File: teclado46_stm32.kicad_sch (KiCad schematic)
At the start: 12 parts, among them J2 78171-0004, U1 XC6206PxxxMR, U2 STM32G474CETx, U4 W25Q128JVS

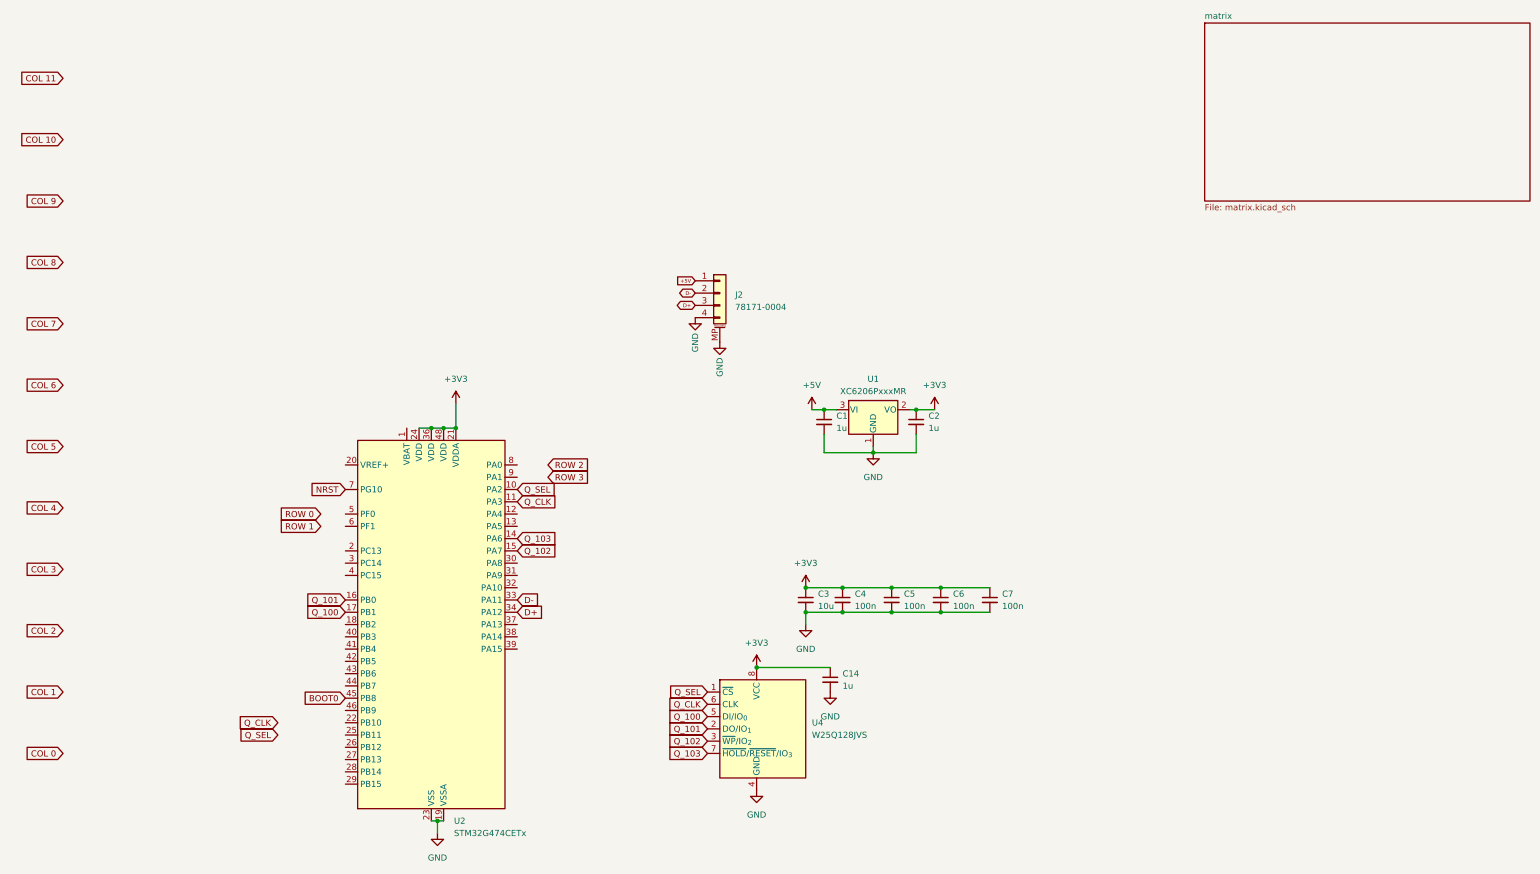
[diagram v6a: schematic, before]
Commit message: chore: routed columns
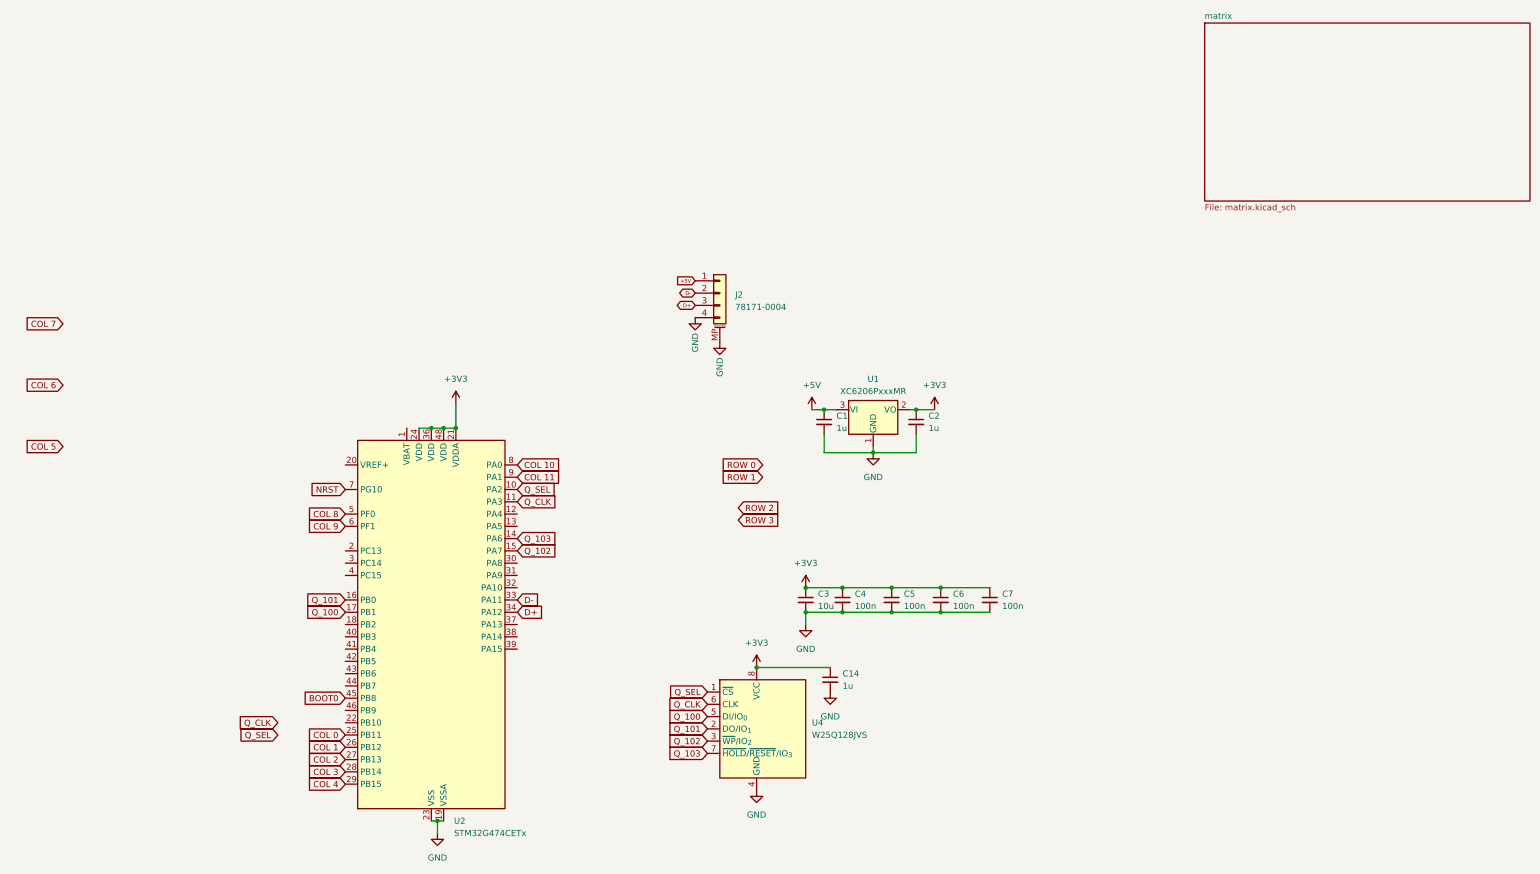
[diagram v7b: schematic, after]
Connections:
- net COL 0: now also U2.25 (PB11)
- net COL 1: now also U2.26 (PB12)
- net COL 10: now also U2.8 (PA0)
- net COL 11: now also U2.9 (PA1)
- net COL 2: now also U2.27 (PB13)
- net COL 3: now also U2.28 (PB14)
- net COL 4: now also U2.29 (PB15)
- net COL 8: now also U2.5 (PF0)
- net COL 9: now also U2.6 (PF1)
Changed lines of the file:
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@@
 	(global_label "COL 2"
 		(shape input)
-		(at -25.4 144.78 180)
-		(fields_autoplaced yes)
-		(effects
-			(font
-				(size 1.27 1.27)
-			)
-			(justify right)
-		)
-		(property "Intersheetrefs" "${INTERSHEET_REFS}"
-			(at -34.1909 144.78 0)
+		(at 33.02 171.45 180)
+		(fields_autoplaced yes)
+		(effects
+			(font
+				(size 1.27 1.27)
+			)
+			(justify right)
+		)
+		(property "Intersheetrefs" "${INTERSHEET_REFS}"
+			(at 24.2291 171.45 0)
 			(effects
 				(font
@@
 	(global_label "ROW 1"
 		(shape input)
-		(at 27.94 123.19 180)
-		(fields_autoplaced yes)
-		(effects
-			(font
-				(size 1.27 1.27)
-			)
-			(justify right)
-		)
-		(property "Intersheetrefs" "${INTERSHEET_REFS}"
-			(at 18.7258 123.19 0)
+		(at 119.38 113.03 180)
+		(fields_autoplaced yes)
+		(effects
+			(font
+				(size 1.27 1.27)
+			)
+			(justify right)
+		)
+		(property "Intersheetrefs" "${INTERSHEET_REFS}"
+			(at 110.1658 113.03 0)
 			(effects
 				(font
@@
 	(global_label "COL 3"
 		(shape input)
-		(at -25.4 132.08 180)
-		(fields_autoplaced yes)
-		(effects
-			(font
-				(size 1.27 1.27)
-			)
-			(justify right)
-		)
-		(property "Intersheetrefs" "${INTERSHEET_REFS}"
-			(at -34.1909 132.08 0)
+		(at 33.02 173.99 180)
+		(fields_autoplaced yes)
+		(effects
+			(font
+				(size 1.27 1.27)
+			)
+			(justify right)
+		)
+		(property "Intersheetrefs" "${INTERSHEET_REFS}"
+			(at 24.2291 173.99 0)
 			(effects
 				(font
@@
 	(global_label "COL 10"
 		(shape input)
-		(at -25.4 43.18 180)
-		(fields_autoplaced yes)
-		(effects
-			(font
-				(size 1.27 1.27)
-			)
-			(justify right)
-		)
-		(property "Intersheetrefs" "${INTERSHEET_REFS}"
-			(at -35.4004 43.18 0)
-			(effects
-				(font
-					(size 1.27 1.27)
-				)
-				(justify right)
+		(at 68.58 110.49 0)
+		(fields_autoplaced yes)
+		(effects
+			(font
+				(size 1.27 1.27)
+			)
+			(justify left)
+		)
+		(property "Intersheetrefs" "${INTERSHEET_REFS}"
+			(at 78.5804 110.49 0)
+			(effects
+				(font
+					(size 1.27 1.27)
+				)
+				(justify left)
 				(hide yes)
 			)
@@
 	(global_label "COL 1"
 		(shape input)
-		(at -25.4 157.48 180)
-		(fields_autoplaced yes)
-		(effects
-			(font
-				(size 1.27 1.27)
-			)
-			(justify right)
-		)
-		(property "Intersheetrefs" "${INTERSHEET_REFS}"
-			(at -34.1909 157.48 0)
+		(at 33.02 168.91 180)
+		(fields_autoplaced yes)
+		(effects
+			(font
+				(size 1.27 1.27)
+			)
+			(justify right)
+		)
+		(property "Intersheetrefs" "${INTERSHEET_REFS}"
+			(at 24.2291 168.91 0)
 			(effects
 				(font
@@
 	(global_label "COL 9"
 		(shape input)
-		(at -25.4 55.88 180)
-		(fields_autoplaced yes)
-		(effects
-			(font
-				(size 1.27 1.27)
-			)
-			(justify right)
-		)
-		(property "Intersheetrefs" "${INTERSHEET_REFS}"
-			(at -34.1909 55.88 0)
+		(at 33.02 123.19 180)
+		(fields_autoplaced yes)
+		(effects
+			(font
+				(size 1.27 1.27)
+			)
+			(justify right)
+		)
+		(property "Intersheetrefs" "${INTERSHEET_REFS}"
+			(at 24.2291 123.19 0)
 			(effects
 				(font
@@
 	(global_label "COL 8"
 		(shape input)
-		(at -25.4 68.58 180)
-		(fields_autoplaced yes)
-		(effects
-			(font
-				(size 1.27 1.27)
-			)
-			(justify right)
-		)
-		(property "Intersheetrefs" "${INTERSHEET_REFS}"
-			(at -34.1909 68.58 0)
+		(at 33.02 120.65 180)
+		(fields_autoplaced yes)
+		(effects
+			(font
+				(size 1.27 1.27)
+			)
+			(justify right)
+		)
+		(property "Intersheetrefs" "${INTERSHEET_REFS}"
+			(at 24.2291 120.65 0)
 			(effects
 				(font
@@
 	(global_label "COL 0"
 		(shape input)
-		(at -25.4 170.18 180)
-		(fields_autoplaced yes)
-		(effects
-			(font
-				(size 1.27 1.27)
-			)
-			(justify right)
-		)
-		(property "Intersheetrefs" "${INTERSHEET_REFS}"
-			(at -34.1909 170.18 0)
+		(at 33.02 166.37 180)
+		(fields_autoplaced yes)
+		(effects
+			(font
+				(size 1.27 1.27)
+			)
+			(justify right)
+		)
+		(property "Intersheetrefs" "${INTERSHEET_REFS}"
+			(at 24.2291 166.37 0)
 			(effects
 				(font
@@
 	(global_label "ROW 0"
 		(shape input)
-		(at 27.94 120.65 180)
-		(fields_autoplaced yes)
-		(effects
-			(font
-				(size 1.27 1.27)
-			)
-			(justify right)
-		)
-		(property "Intersheetrefs" "${INTERSHEET_REFS}"
-			(at 18.7258 120.65 0)
+		(at 119.38 110.49 180)
+		(fields_autoplaced yes)
+		(effects
+			(font
+				(size 1.27 1.27)
+			)
+			(justify right)
+		)
+		(property "Intersheetrefs" "${INTERSHEET_REFS}"
+			(at 110.1658 110.49 0)
 			(effects
 				(font
@@
 	(global_label "ROW 2"
 		(shape input)
-		(at 74.93 110.49 0)
-		(fields_autoplaced yes)
-		(effects
-			(font
-				(size 1.27 1.27)
-			)
-			(justify left)
-		)
-		(property "Intersheetrefs" "${INTERSHEET_REFS}"
-			(at 84.1442 110.49 0)
+		(at 114.3 119.38 0)
+		(fields_autoplaced yes)
+		(effects
+			(font
+				(size 1.27 1.27)
+			)
+			(justify left)
+		)
+		(property "Intersheetrefs" "${INTERSHEET_REFS}"
+			(at 123.5142 119.38 0)
 			(effects
 				(font
@@
 	(global_label "COL 4"
 		(shape input)
-		(at -25.4 119.38 180)
-		(fields_autoplaced yes)
-		(effects
-			(font
-				(size 1.27 1.27)
-			)
-			(justify right)
-		)
-		(property "Intersheetrefs" "${INTERSHEET_REFS}"
-			(at -34.1909 119.38 0)
+		(at 33.02 176.53 180)
+		(fields_autoplaced yes)
+		(effects
+			(font
+				(size 1.27 1.27)
+			)
+			(justify right)
+		)
+		(property "Intersheetrefs" "${INTERSHEET_REFS}"
+			(at 24.2291 176.53 0)
 			(effects
 				(font
@@
 	(global_label "COL 11"
 		(shape input)
-		(at -25.4 30.48 180)
-		(fields_autoplaced yes)
-		(effects
-			(font
-				(size 1.27 1.27)
-			)
-			(justify right)
-		)
-		(property "Intersheetrefs" "${INTERSHEET_REFS}"
-			(at -35.4004 30.48 0)
-			(effects
-				(font
-					(size 1.27 1.27)
-				)
-				(justify right)
+		(at 68.58 113.03 0)
+		(fields_autoplaced yes)
+		(effects
+			(font
+				(size 1.27 1.27)
+			)
+			(justify left)
+		)
+		(property "Intersheetrefs" "${INTERSHEET_REFS}"
+			(at 78.5804 113.03 0)
+			(effects
+				(font
+					(size 1.27 1.27)
+				)
+				(justify left)
 				(hide yes)
 			)
@@
 	(global_label "ROW 3"
 		(shape input)
-		(at 74.93 113.03 0)
-		(fields_autoplaced yes)
-		(effects
-			(font
-				(size 1.27 1.27)
-			)
-			(justify left)
-		)
-		(property "Intersheetrefs" "${INTERSHEET_REFS}"
-			(at 84.1442 113.03 0)
-			(effects
-				(font
+		(at 114.3 121.92 0)
+		(fields_autoplaced yes)
+		(effects
+			(font
+				(size 1.27 1.27)
+			)
+			(justify left)
+		)
+		(property "Intersheetrefs" "${INTERSHEET_REFS}"
+			(at 123.5142 121.92 0)
+			(effects
+				(font

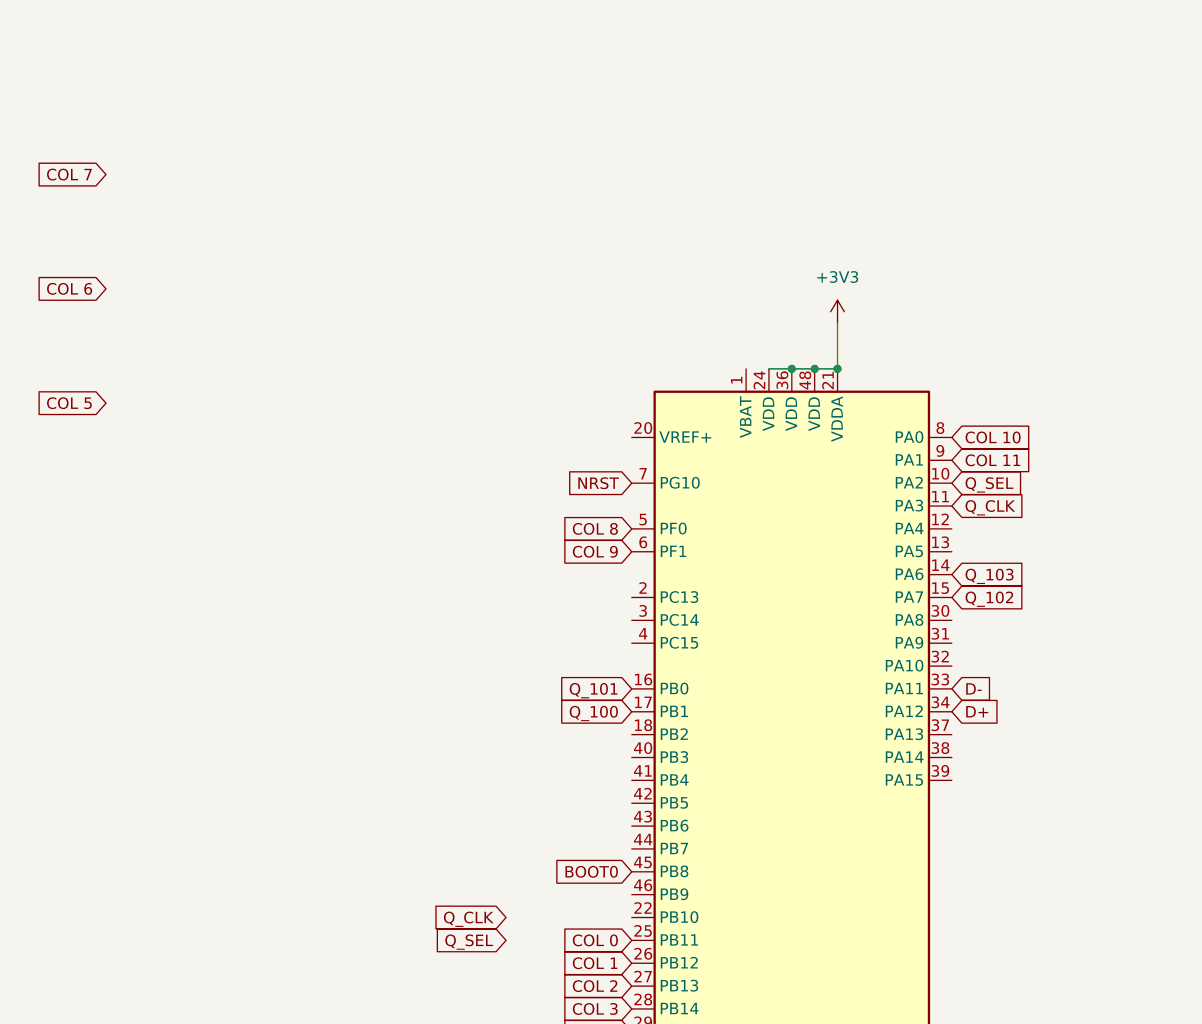
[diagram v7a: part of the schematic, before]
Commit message: chore: routed all columns
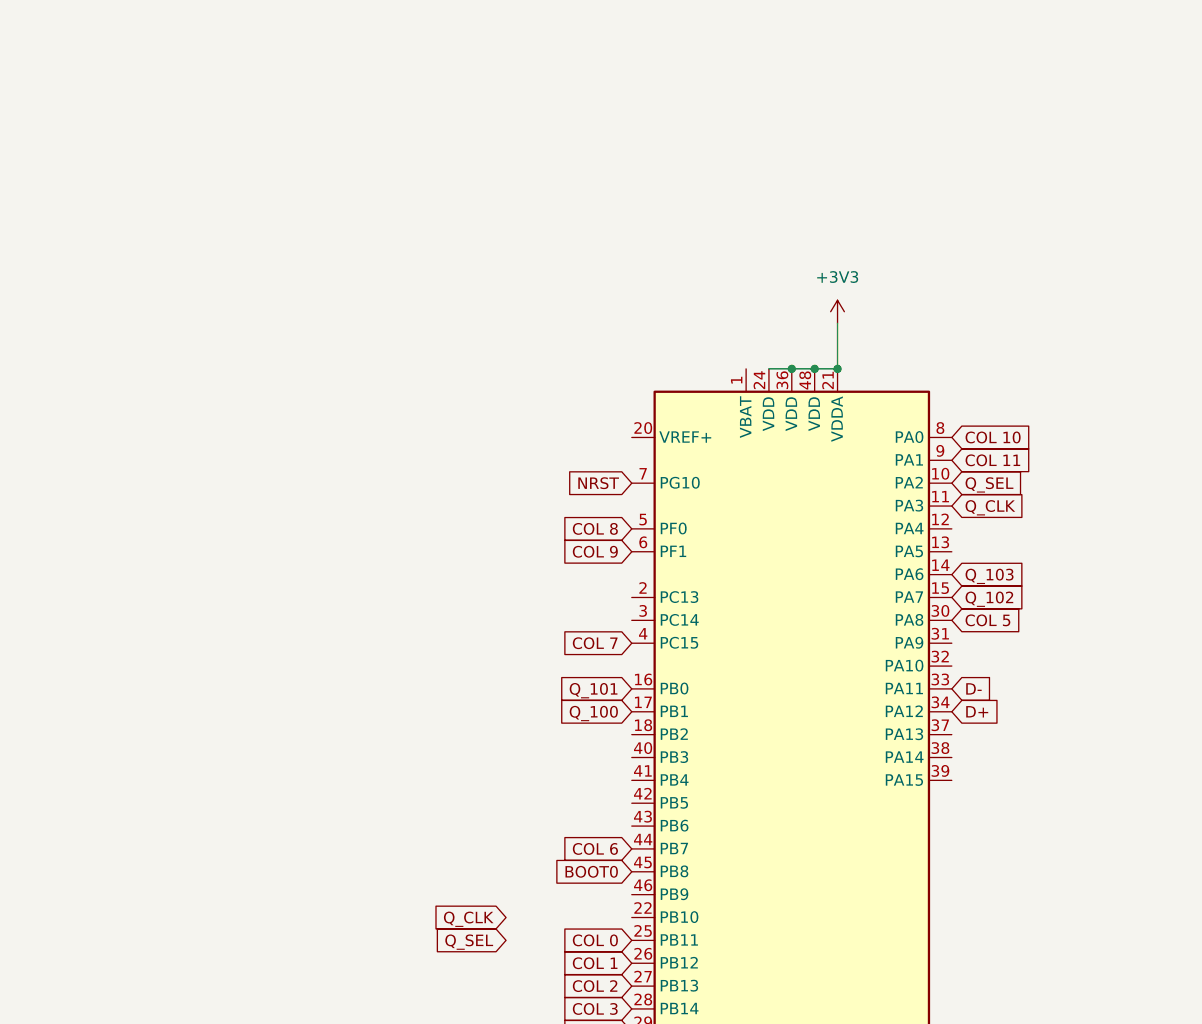
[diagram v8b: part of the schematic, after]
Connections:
- net COL 5: now also U2.30 (PA8)
- net COL 6: now also U2.44 (PB7)
- net COL 7: now also U2.4 (PC15)
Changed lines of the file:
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@@
 	(global_label "COL 6"
 		(shape input)
-		(at -25.4 93.98 180)
-		(fields_autoplaced yes)
-		(effects
-			(font
-				(size 1.27 1.27)
-			)
-			(justify right)
-		)
-		(property "Intersheetrefs" "${INTERSHEET_REFS}"
-			(at -34.1909 93.98 0)
+		(at 33.02 156.21 180)
+		(fields_autoplaced yes)
+		(effects
+			(font
+				(size 1.27 1.27)
+			)
+			(justify right)
+		)
+		(property "Intersheetrefs" "${INTERSHEET_REFS}"
+			(at 24.2291 156.21 0)
 			(effects
 				(font
@@
 	(global_label "COL 5"
 		(shape input)
-		(at -25.4 106.68 180)
-		(fields_autoplaced yes)
-		(effects
-			(font
-				(size 1.27 1.27)
-			)
-			(justify right)
-		)
-		(property "Intersheetrefs" "${INTERSHEET_REFS}"
-			(at -34.1909 106.68 0)
-			(effects
-				(font
-					(size 1.27 1.27)
-				)
-				(justify right)
+		(at 68.58 130.81 0)
+		(fields_autoplaced yes)
+		(effects
+			(font
+				(size 1.27 1.27)
+			)
+			(justify left)
+		)
+		(property "Intersheetrefs" "${INTERSHEET_REFS}"
+			(at 77.3709 130.81 0)
+			(effects
+				(font
+					(size 1.27 1.27)
+				)
+				(justify left)
 				(hide yes)
 			)
@@
 	(global_label "COL 7"
 		(shape input)
-		(at -25.4 81.28 180)
-		(fields_autoplaced yes)
-		(effects
-			(font
-				(size 1.27 1.27)
-			)
-			(justify right)
-		)
-		(property "Intersheetrefs" "${INTERSHEET_REFS}"
-			(at -34.1909 81.28 0)
-			(effects
-				(font
+		(at 33.02 133.35 180)
+		(fields_autoplaced yes)
+		(effects
+			(font
+				(size 1.27 1.27)
+			)
+			(justify right)
+		)
+		(property "Intersheetrefs" "${INTERSHEET_REFS}"
+			(at 24.2291 133.35 0)
+			(effects
+				(font
